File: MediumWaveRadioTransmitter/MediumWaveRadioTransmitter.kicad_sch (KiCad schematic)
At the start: 17 parts, among them J1 Screw_Terminal_01x05, Q1 BC337, Q2 BC337, Y1 400 kH

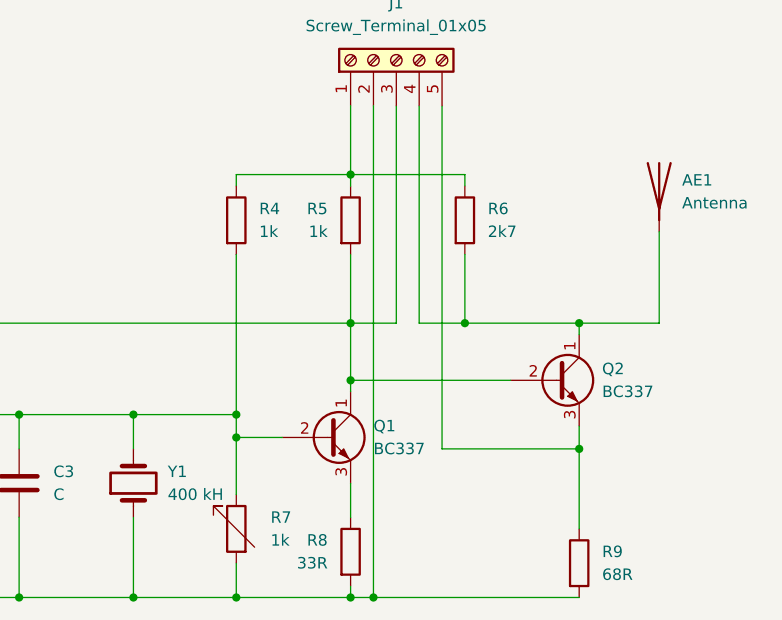
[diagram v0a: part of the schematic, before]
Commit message: feat: circuit diagram improved
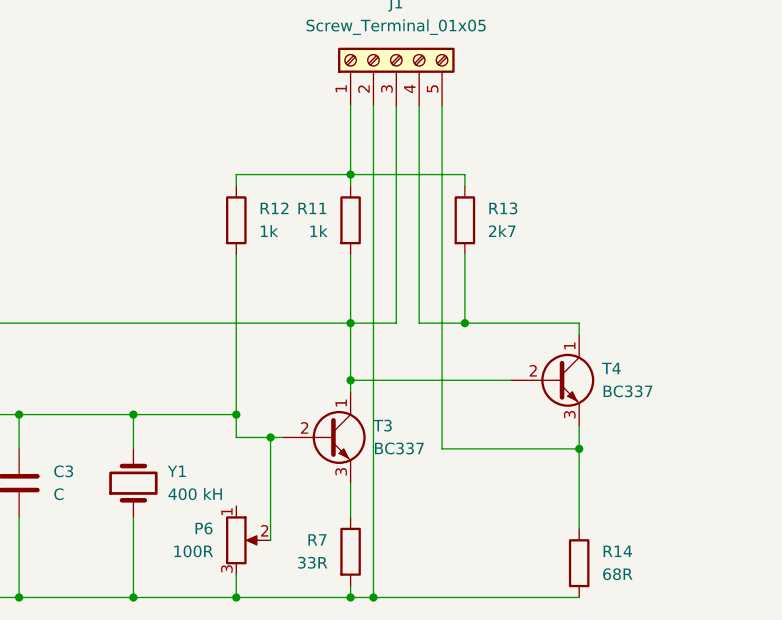
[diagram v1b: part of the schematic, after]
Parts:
- removed AE1: Antenna, symbol Device:Antenna
- removed R7: 1k, Resistor_THT:R_Axial_DIN0204_L3.6mm_D1.6mm_P1.90mm_Vertical, symbol Device:R_Variable
- added P6: 100R, Potentiometer_THT:Potentiometer_Bourns_3296W_Vertical, symbol Device:R_Potentiometer
- C1, C2, C3: footprint (none) -> Capacitor_THT:C_Disc_D3.0mm_W1.6mm_P2.50mm
- T3: renamed from Q1; footprint Package_TO_SOT_THT:TO-92_Inline -> Package_TO_SOT_THT:TO-92
- T4: renamed from Q2; footprint Package_TO_SOT_THT:TO-92_Inline -> Package_TO_SOT_THT:TO-92
- Y1: footprint Crystal:Crystal_HC50_Vertical -> Crystal:Resonator-2Pin_W8.0mm_H3.5mm
- renumbered R5 to R11, R4 to R12, R6 to R13, R9 to R14, R8 to R7
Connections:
- net at C1.2, C2.2, C3.2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: now also P6.3
- net at C3.1, R12.2, R3.2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: now also P6.2

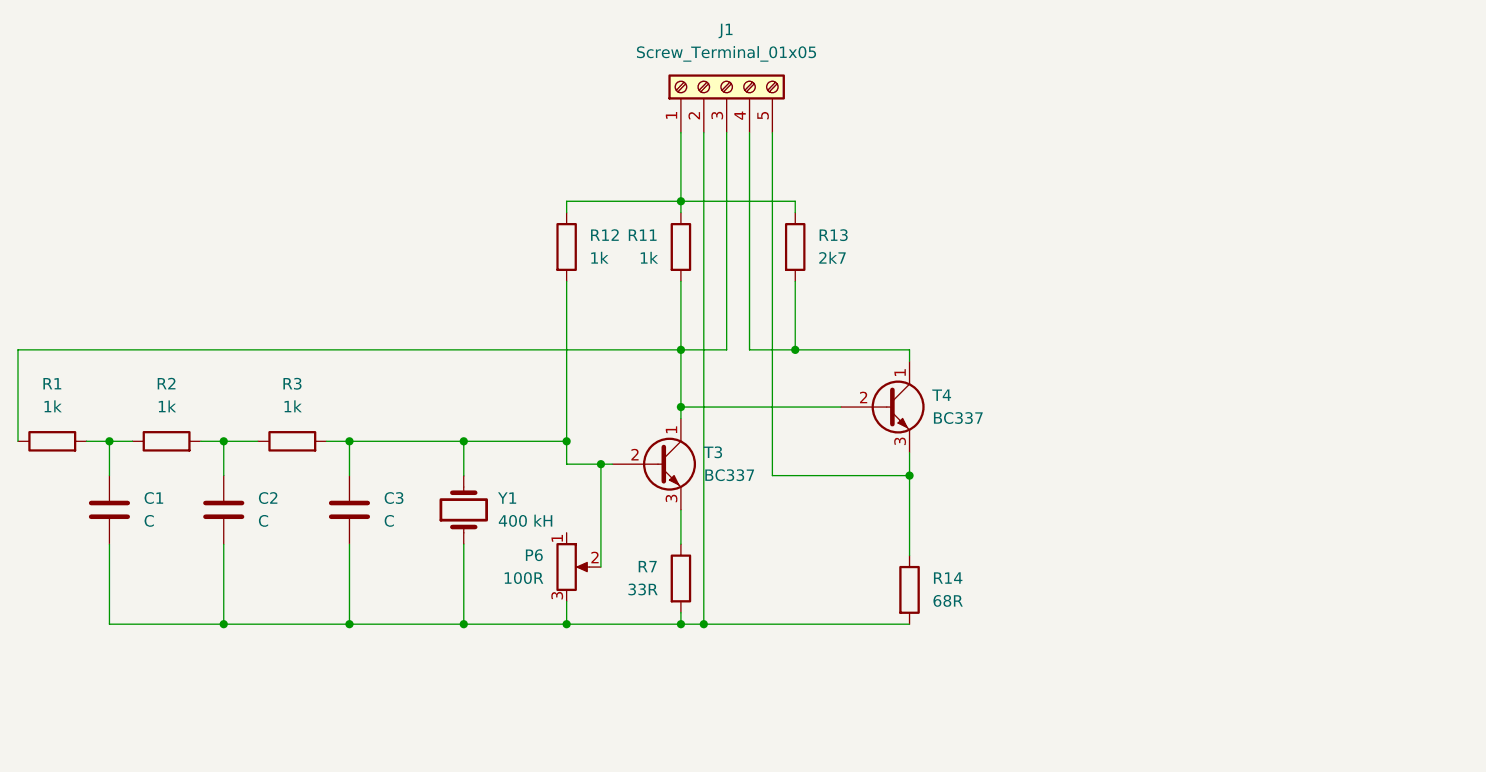
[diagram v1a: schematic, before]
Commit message: feat: circuit diagram improved
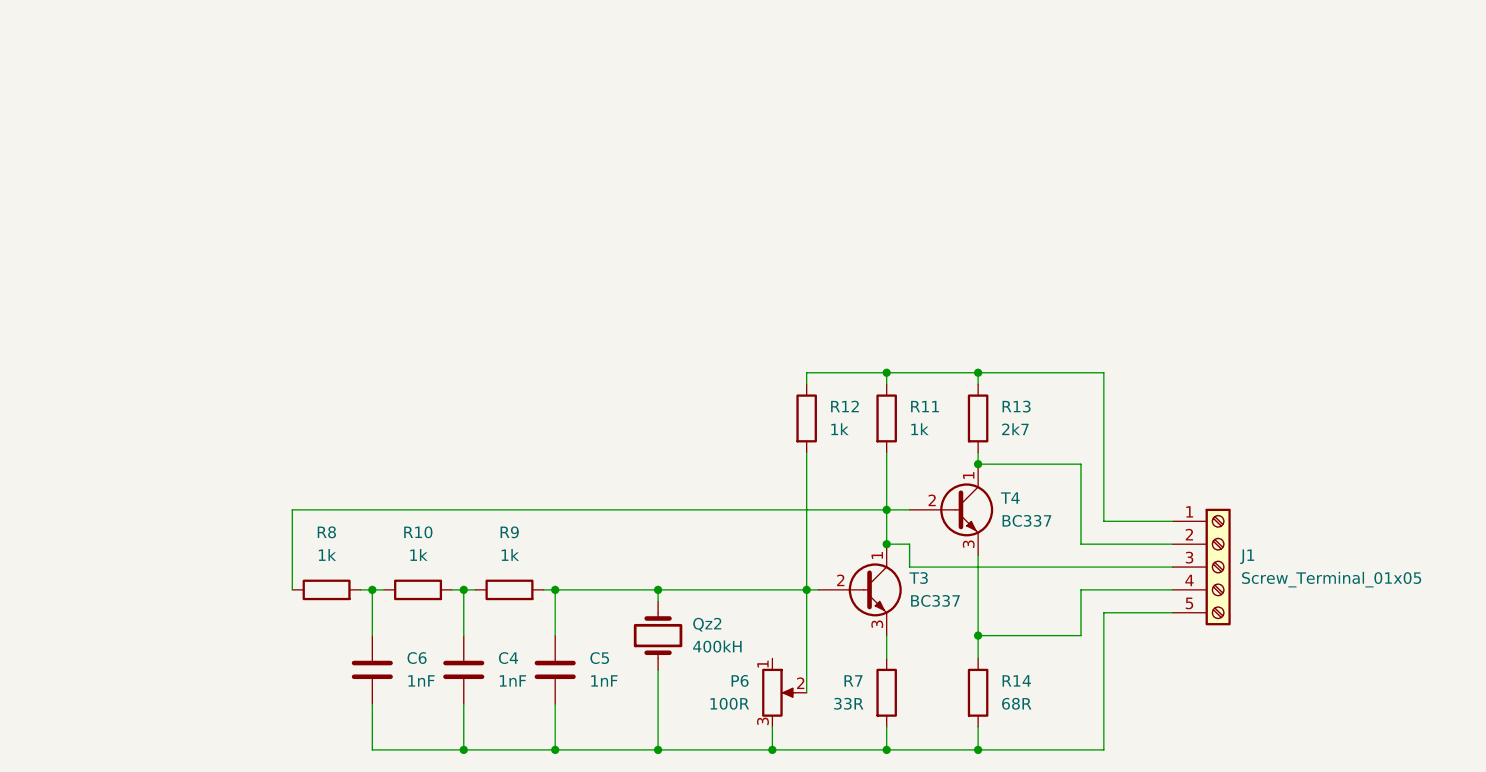
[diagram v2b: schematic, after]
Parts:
- C4: renamed from C2; value C -> 1nF
- C5: renamed from C3; value C -> 1nF
- C6: renamed from C1; value C -> 1nF
- Qz2: renamed from Y1; value 400 kH -> 400kH
- renumbered R2 to R10, R1 to R8, R3 to R9
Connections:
- net at C4.2, C5.2, C6.2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: now also J1.5 (Pin_5); no longer J1.2 (Pin_2)
- net at R13.2, T4.1 (C): now also J1.2 (Pin_2); no longer J1.4 (Pin_4)
- net at R14.1, T4.3 (E): now also J1.4 (Pin_4); no longer J1.5 (Pin_5)
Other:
- moved on the sheet: C4, C5, C6, J1, P6, Qz2, R10, R12, R13, R14, R7, R8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

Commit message: feat: circuit diagram improved
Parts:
- C4, C5: footprint Capacitor_THT:C_Disc_D3.0mm_W1.6mm_P2.50mm -> Capacitor_THT:C_Disc_D4.3mm_W1.9mm_P5.00mm
- C6: footprint Capacitor_THT:C_Disc_D3.0mm_W1.6mm_P2.50mm -> Capacitor_THT:C_Disc_D4.7mm_W2.5mm_P5.00mm
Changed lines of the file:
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@@
       (effects (font (size 1.27 1.27)) (justify left))
     )
-    (property "Footprint" "Capacitor_THT:C_Disc_D3.0mm_W1.6mm_P2.50mm" (at 93.6752 116.84 0)
-      (effects (font (size 1.27 1.27)) hide)
-    )
-    (property "Datasheet" "~" (at 92.71 113.03 0)
+    (property "Footprint" "Capacitor_THT:C_Disc_D4.7mm_W2.5mm_P5.00mm" (at 93.6752 116.84 0)
+      (effects (font (size 1.27 1.27)) hide)
+    )
+    (property "Datasheet" "https://cdn-reichelt.de/documents/datenblatt/B300/KERKO500_TDP.pdf" (at 92.71 113.03 0)
       (effects (font (size 1.27 1.27)) hide)
     )
@@
       (effects (font (size 1.27 1.27)) (justify left))
     )
-    (property "Footprint" "Capacitor_THT:C_Disc_D3.0mm_W1.6mm_P2.50mm" (at 103.8352 116.84 0)
-      (effects (font (size 1.27 1.27)) hide)
-    )
-    (property "Datasheet" "~" (at 102.87 113.03 0)
+    (property "Footprint" "Capacitor_THT:C_Disc_D4.3mm_W1.9mm_P5.00mm" (at 103.8352 116.84 0)
+      (effects (font (size 1.27 1.27)) hide)
+    )
+    (property "Datasheet" "https://cdn-reichelt.de/documents/datenblatt/B300/KERKO500_TDP.pdf" (at 102.87 113.03 0)
       (effects (font (size 1.27 1.27)) hide)
     )
@@
       (effects (font (size 1.27 1.27)) (justify left))
     )
-    (property "Footprint" "Capacitor_THT:C_Disc_D3.0mm_W1.6mm_P2.50mm" (at 113.9952 116.84 0)
-      (effects (font (size 1.27 1.27)) hide)
-    )
-    (property "Datasheet" "~" (at 113.03 113.03 0)
+    (property "Footprint" "Capacitor_THT:C_Disc_D4.3mm_W1.9mm_P5.00mm" (at 113.9952 116.84 0)
+      (effects (font (size 1.27 1.27)) hide)
+    )
+    (property "Datasheet" "https://cdn-reichelt.de/documents/datenblatt/B300/KERKO500_TDP.pdf" (at 113.03 113.03 0)
       (effects (font (size 1.27 1.27)) hide)
     )
@@
       (effects (font (size 1.27 1.27)) hide)
     )
-    (property "Datasheet" "~" (at 124.46 109.22 0)
-      (effects (font (size 1.27 1.27)) hide)
-    )
+    (property "Datasheet" "https://ecsxtal.com/store/pdf/ztb_ztbfr.pdf" (at 124.46 109.22 0)
+      (effects (font (size 1.27 1.27)) hide)
+    )

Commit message: feat: circuit diagram improved
changes:
- circuit diagram improved
- pcb layout routed

closes #1
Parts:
- C4, C5: footprint Capacitor_THT:C_Disc_D4.3mm_W1.9mm_P5.00mm -> Capacitor_THT:C_Disc_D4.7mm_W2.5mm_P5.00mm
- J1: value Screw_Terminal_01x05 -> WAGO 734-135
- R10, R11, R12, R13, R14, R7, R8, R9: footprint Resistor_THT:R_Axial_DIN0204_L3.6mm_D1.6mm_P1.90mm_Vertical -> Resistor_THT:R_Axial_DIN0207_L6.3mm_D2.5mm_P7.62mm_Horizontal
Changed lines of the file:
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@@
       (effects (font (size 1.27 1.27)))
     )
-    (property "Footprint" "Resistor_THT:R_Axial_DIN0204_L3.6mm_D1.6mm_P1.90mm_Vertical" (at 97.79 105.918 90)
+    (property "Footprint" "Resistor_THT:R_Axial_DIN0207_L6.3mm_D2.5mm_P7.62mm_Horizontal" (at 97.79 105.918 90)
       (effects (font (size 1.27 1.27)) hide)
     )
@@
       (effects (font (size 1.27 1.27)) (justify left))
     )
-    (property "Value" "Screw_Terminal_01x05" (at 189.23 102.87 0)
+    (property "Value" "WAGO 734-135" (at 189.23 102.87 0)
       (effects (font (size 1.27 1.27)) (justify left))
     )
@@
       (effects (font (size 1.27 1.27)) (justify left))
     )
-    (property "Footprint" "Capacitor_THT:C_Disc_D4.3mm_W1.9mm_P5.00mm" (at 103.8352 116.84 0)
+    (property "Footprint" "Capacitor_THT:C_Disc_D4.7mm_W2.5mm_P5.00mm" (at 103.8352 116.84 0)
       (effects (font (size 1.27 1.27)) hide)
     )
@@
       (effects (font (size 1.27 1.27)))
     )
-    (property "Footprint" "Resistor_THT:R_Axial_DIN0204_L3.6mm_D1.6mm_P1.90mm_Vertical" (at 87.63 105.918 90)
+    (property "Footprint" "Resistor_THT:R_Axial_DIN0207_L6.3mm_D2.5mm_P7.62mm_Horizontal" (at 87.63 105.918 90)
       (effects (font (size 1.27 1.27)) hide)
     )
@@
       (effects (font (size 1.27 1.27)))
     )
-    (property "Footprint" "Resistor_THT:R_Axial_DIN0204_L3.6mm_D1.6mm_P1.90mm_Vertical" (at 107.95 105.918 90)
+    (property "Footprint" "Resistor_THT:R_Axial_DIN0207_L6.3mm_D2.5mm_P7.62mm_Horizontal" (at 107.95 105.918 90)
       (effects (font (size 1.27 1.27)) hide)
     )
@@
       (effects (font (size 1.27 1.27)) (justify left))
     )
-    (property "Footprint" "Resistor_THT:R_Axial_DIN0204_L3.6mm_D1.6mm_P1.90mm_Vertical" (at 139.192 85.09 90)
+    (property "Footprint" "Resistor_THT:R_Axial_DIN0207_L6.3mm_D2.5mm_P7.62mm_Horizontal" (at 139.192 85.09 90)
       (effects (font (size 1.27 1.27)) hide)
     )
@@
       (effects (font (size 1.27 1.27)) (justify left))
     )
-    (property "Footprint" "Resistor_THT:R_Axial_DIN0204_L3.6mm_D1.6mm_P1.90mm_Vertical" (at 158.242 85.09 90)
+    (property "Footprint" "Resistor_THT:R_Axial_DIN0207_L6.3mm_D2.5mm_P7.62mm_Horizontal" (at 158.242 85.09 90)
       (effects (font (size 1.27 1.27)) hide)
     )
@@
       (effects (font (size 1.27 1.27)) (justify left))
     )
-    (property "Footprint" "Resistor_THT:R_Axial_DIN0204_L3.6mm_D1.6mm_P1.90mm_Vertical" (at 158.242 115.57 90)
+    (property "Footprint" "Resistor_THT:R_Axial_DIN0207_L6.3mm_D2.5mm_P7.62mm_Horizontal" (at 158.242 115.57 90)
       (effects (font (size 1.27 1.27)) hide)
     )
@@
       (effects (font (size 1.27 1.27)) (justify left))
     )
-    (property "Footprint" "Capacitor_THT:C_Disc_D4.3mm_W1.9mm_P5.00mm" (at 113.9952 116.84 0)
+    (property "Footprint" "Capacitor_THT:C_Disc_D4.7mm_W2.5mm_P5.00mm" (at 113.9952 116.84 0)
       (effects (font (size 1.27 1.27)) hide)
     )
@@
       (effects (font (size 1.27 1.27)) (justify right))
     )
-    (property "Footprint" "Resistor_THT:R_Axial_DIN0204_L3.6mm_D1.6mm_P1.90mm_Vertical" (at 148.082 115.57 90)
+    (property "Footprint" "Resistor_THT:R_Axial_DIN0207_L6.3mm_D2.5mm_P7.62mm_Horizontal" (at 148.082 115.57 90)
       (effects (font (size 1.27 1.27)) hide)
     )
@@
       (effects (font (size 1.27 1.27)) (justify left))
     )
-    (property "Footprint" "Resistor_THT:R_Axial_DIN0204_L3.6mm_D1.6mm_P1.90mm_Vertical" (at 148.082 85.09 90)
-      (effects (font (size 1.27 1.27)) hide)
-    )
+    (property "Footprint" "Resistor_THT:R_Axial_DIN0207_L6.3mm_D2.5mm_P7.62mm_Horizontal" (at 148.082 85.09 90)
+      (effects (font (size 1.27 1.27)) hide)
+    )
